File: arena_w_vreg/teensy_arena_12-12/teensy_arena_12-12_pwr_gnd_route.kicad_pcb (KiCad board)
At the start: 4 copper layers, 254 x 254 mm, 87 parts, among them J1 Barrel_Jack, J2 Conn_01x04, J3 Conn_01x04, P1 CONN15, P10 CONN15, P11 CONN15, P12 CONN15, P2 CONN15, P3 CONN15, P4 CONN15, P5 CONN15, P6 CONN15, P7 CONN15, P8 CONN15, P9 CONN15, Q2 MOSFET_NCHAN, SW1 SW_SPDT, U1 TXB0108PW, U10 AZ1084-5.0, U11 AZ1084-5.0, U12 AZ1084-5.0, U13 AZ1084-5.0, U14 AZ1084-5.0, U15 AZ1084-5.0, U16 AZ1084-5.0, U17 AZ1084-5.0, U18 Teensy4.1, U2 TXB0108PW, U3 TXB0108PW, U4 TXB0108PW, U5 TXB0108PW, U6 AZ1084-5.0, U7 AZ1084-5.0, U8 AZ1084-5.0, U9 AZ1084-5.0

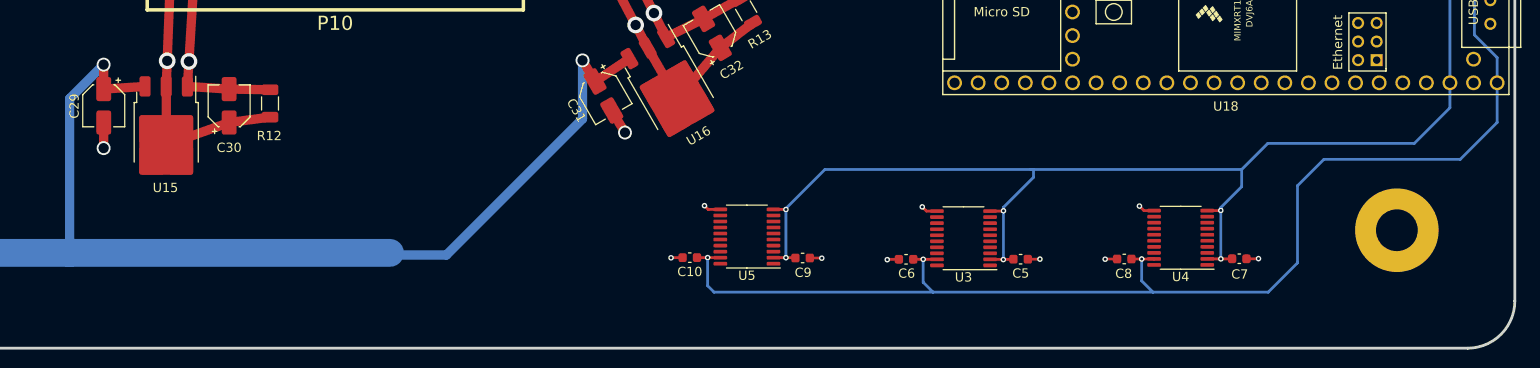
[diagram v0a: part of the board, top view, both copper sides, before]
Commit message: Worked on routing 12-12 arena with vreg.
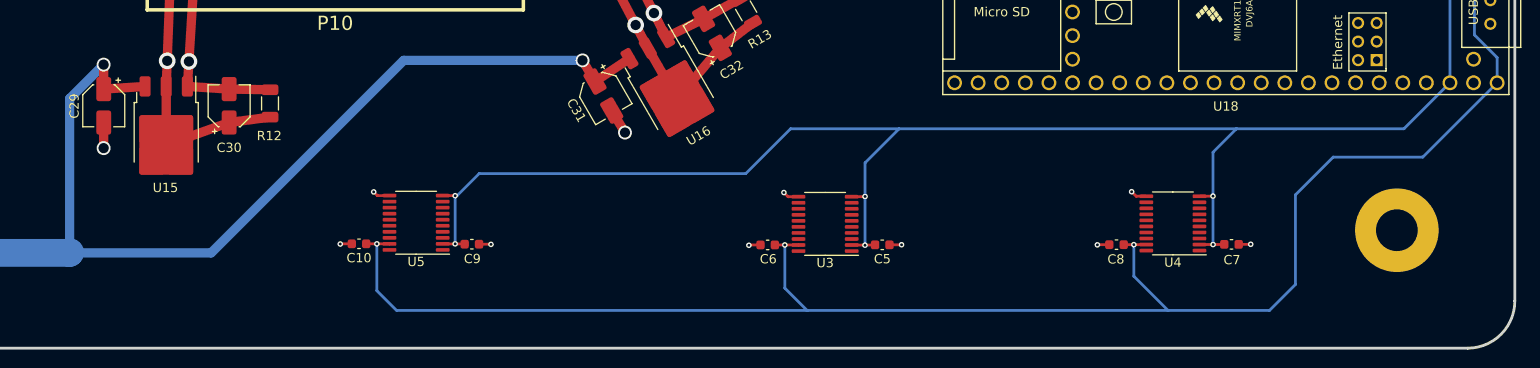
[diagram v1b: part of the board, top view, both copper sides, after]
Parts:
- moved C9 35.6 mm to (192.5, 293.6)
- moved U5 35.6 mm to (186.5, 291.3)
- moved C10 35.6 mm to (180.4, 293.6)
- moved C5 15.0 mm to (236.7, 293.7)
- moved C6 15.0 mm to (224.4, 293.7)
- moved U3 15.0 mm to (230.5, 291.4)
- moved C7 1.76 mm to (274.3, 293.6)
- moved C8 1.76 mm to (261.9, 293.7)
- moved U4 1.76 mm to (268.0, 291.4)
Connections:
- P1 pad 3: /Level Shifters/PAN5V.SCK_1 -> /Panel Headers/RESET
- P10 pad 3: /Level Shifters/PAN5V.SCK_1 -> /Panel Headers/RESET
- P11 pad 3: /Level Shifters/PAN5V.SCK_1 -> /Panel Headers/RESET
- P12 pad 3: /Level Shifters/PAN5V.SCK_1 -> /Panel Headers/RESET
- P2 pad 3: /Level Shifters/PAN5V.SCK_1 -> /Panel Headers/RESET
- P3 pad 3: /Level Shifters/PAN5V.SCK_1 -> /Panel Headers/RESET
- P4 pad 3: /Level Shifters/PAN5V.SCK_1 -> /Panel Headers/RESET
- P5 pad 3: /Level Shifters/PAN5V.SCK_1 -> /Panel Headers/RESET
- P6 pad 3: /Level Shifters/PAN5V.SCK_1 -> /Panel Headers/RESET
- P7 pad 3: /Level Shifters/PAN5V.SCK_1 -> /Panel Headers/RESET
- P8 pad 3: /Level Shifters/PAN5V.SCK_1 -> /Panel Headers/RESET
- P9 pad 3: /Level Shifters/PAN5V.SCK_1 -> /Panel Headers/RESET
- Q2 pad 3: /Level Shifters/PAN5V.SCK_1 -> /Panel Headers/RESET
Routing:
- net +5V: track 189.9 -> 235.9 mm
- net +3.3V: track 229.8 -> 269.0 mm
- net VCC: track 1076.0 -> 1072.1 mm

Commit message: Added new pcb routing for 12-12 with vreg.
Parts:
- J2, J3: footprint Connector_JST:JST_SH_SM04B-SRSS-TB_1x04-1MP_P1.00mm_Horizontal -> arena_custom:JST_SH_SM04B-SRSS-TB_1x04-1MP_P1.00mm_Horizontal
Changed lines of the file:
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@@
     )
   )
-  (footprint "Connector_JST:JST_SH_SM04B-SRSS-TB_1x04-1MP_P1.00mm_Horizontal" (layer "F.Cu")
+  (footprint "arena_custom:JST_SH_SM04B-SRSS-TB_1x04-1MP_P1.00mm_Horizontal" (layer "F.Cu")
     (at 301.625 230.505 90)
     (descr "JST SH series connector, SM04B-SRSS-TB (http://www.jst-mfg.com/product/pdf/eng/eSH.pdf), generated with kicad-footprint-generator")
@@
     (pad "MP" smd roundrect (at -2.8 1.875 90) (size 1.2 1.8) (layers "F.Cu" "F.Paste" "F.Mask") (roundrect_rratio 0.208333))
     (pad "MP" smd roundrect (at 2.8 1.875 90) (size 1.2 1.8) (layers "F.Cu" "F.Paste" "F.Mask") (roundrect_rratio 0.208333))
-    (model "${KICAD6_3DMODEL_DIR}/Connector_JST.3dshapes/JST_SH_SM04B-SRSS-TB_1x04-1MP_P1.00mm_Horizontal.wrl"
-      (offset (xyz 0 0 0))
+    (model "${KIPRJMOD}/arena_custom.pretty/3d_models/StemmaQT-SM04B-SRSS-TB.step"
+      (offset (xyz 0 1.2 0))
       (scale (xyz 1 1 1))
-      (rotate (xyz 0 0 0))
+      (rotate (xyz -90 0 0))
     )
   )
@@
     )
   )
-  (footprint "Connector_JST:JST_SH_SM04B-SRSS-TB_1x04-1MP_P1.00mm_Horizontal" (layer "F.Cu")
+  (footprint "arena_custom:JST_SH_SM04B-SRSS-TB_1x04-1MP_P1.00mm_Horizontal" (layer "F.Cu")
     (at 301.655 239.516 90)
     (descr "JST SH series connector, SM04B-SRSS-TB (http://www.jst-mfg.com/product/pdf/eng/eSH.pdf), generated with kicad-footprint-generator")
@@
     (pad "MP" smd roundrect (at -2.8 1.875 90) (size 1.2 1.8) (layers "F.Cu" "F.Paste" "F.Mask") (roundrect_rratio 0.208333))
     (pad "MP" smd roundrect (at 2.8 1.875 90) (size 1.2 1.8) (layers "F.Cu" "F.Paste" "F.Mask") (roundrect_rratio 0.208333))
-    (model "${KICAD6_3DMODEL_DIR}/Connector_JST.3dshapes/JST_SH_SM04B-SRSS-TB_1x04-1MP_P1.00mm_Horizontal.wrl"
-      (offset (xyz 0 0 0))
+    (model "${KIPRJMOD}/arena_custom.pretty/3d_models/StemmaQT-SM04B-SRSS-TB.step"
+      (offset (xyz 0 1.2 0))
       (scale (xyz 1 1 1))
-      (rotate (xyz 0 0 0))
+      (rotate (xyz -90 0 0))
     )
   )
